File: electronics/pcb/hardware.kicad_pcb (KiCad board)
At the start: 4 copper layers, 59 x 53 mm, 145 parts, among them J1 Micro_SD_Card_Det_Hirose_DM3AT, J2 USB_A, J3 USB_A, J5 Conn_02x10_Odd_Even, U1 AS4C512M16D3L-12BIN, U2 A33, U3 TPS62095RGTR, U4 TPS62095RGTR, U5 TPS62095RGTR, U6 TPS62095RGTR, U7 AP131-25, Y1 24Mhz, Y2 32.768khz

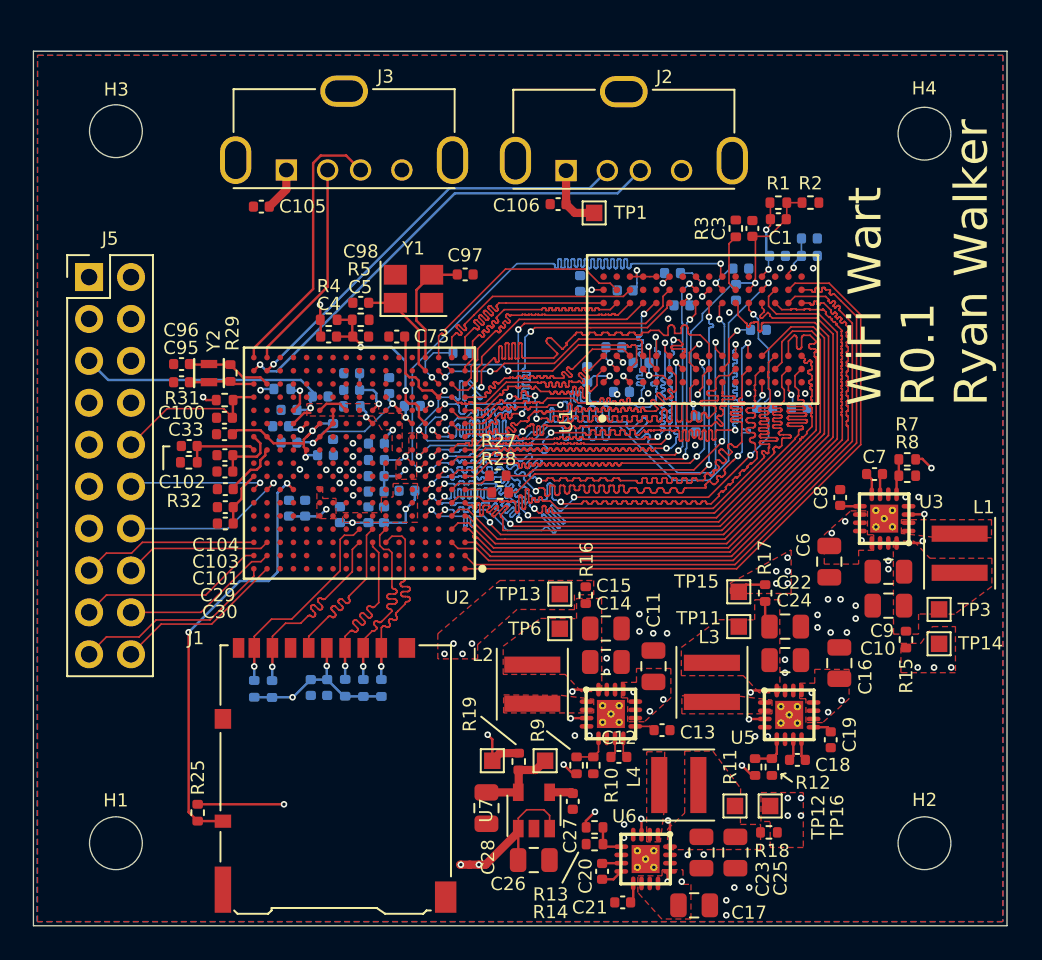
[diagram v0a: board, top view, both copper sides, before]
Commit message: Rendered more gerbers
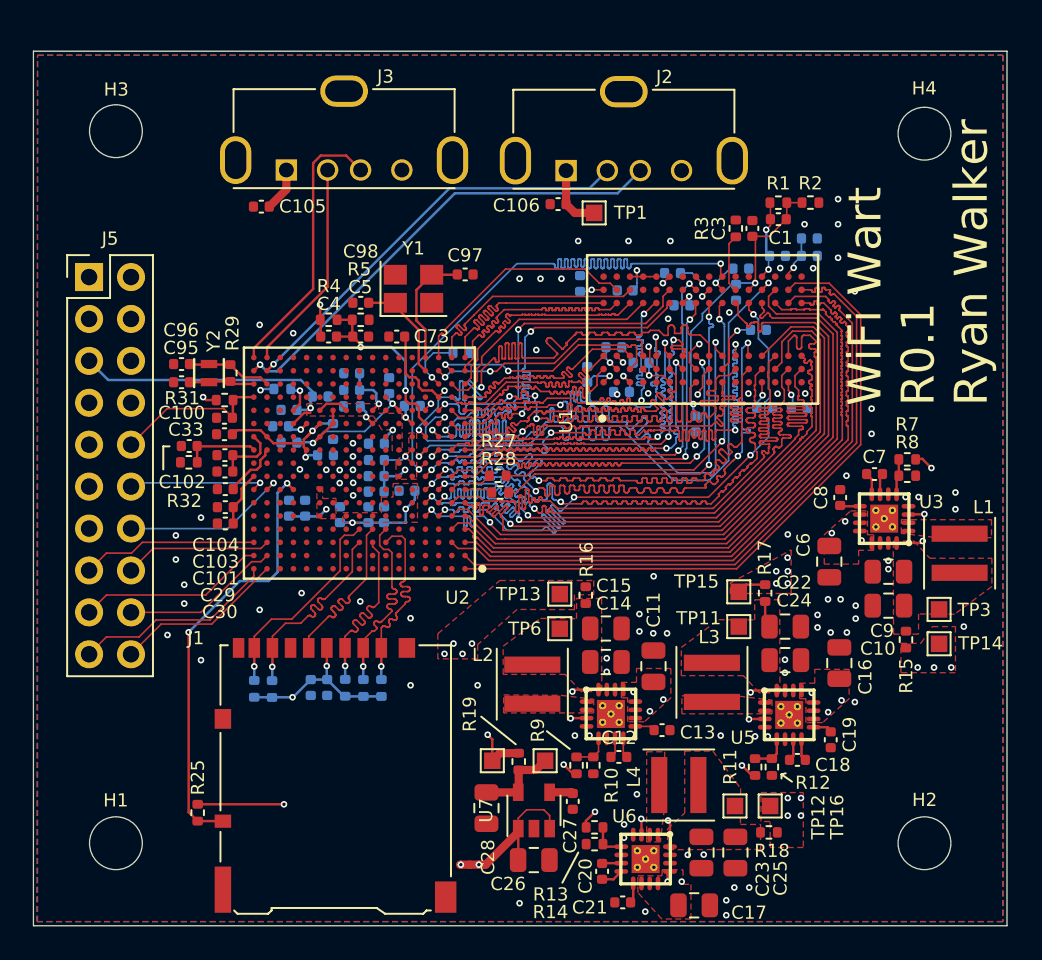
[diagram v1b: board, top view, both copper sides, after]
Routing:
- net GND: vias 57 -> 96
- net +3V0: vias 7 -> 8
